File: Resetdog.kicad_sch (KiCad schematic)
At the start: 14 parts, among them U14 MC14541BD, U15 MC74HC4538ADG

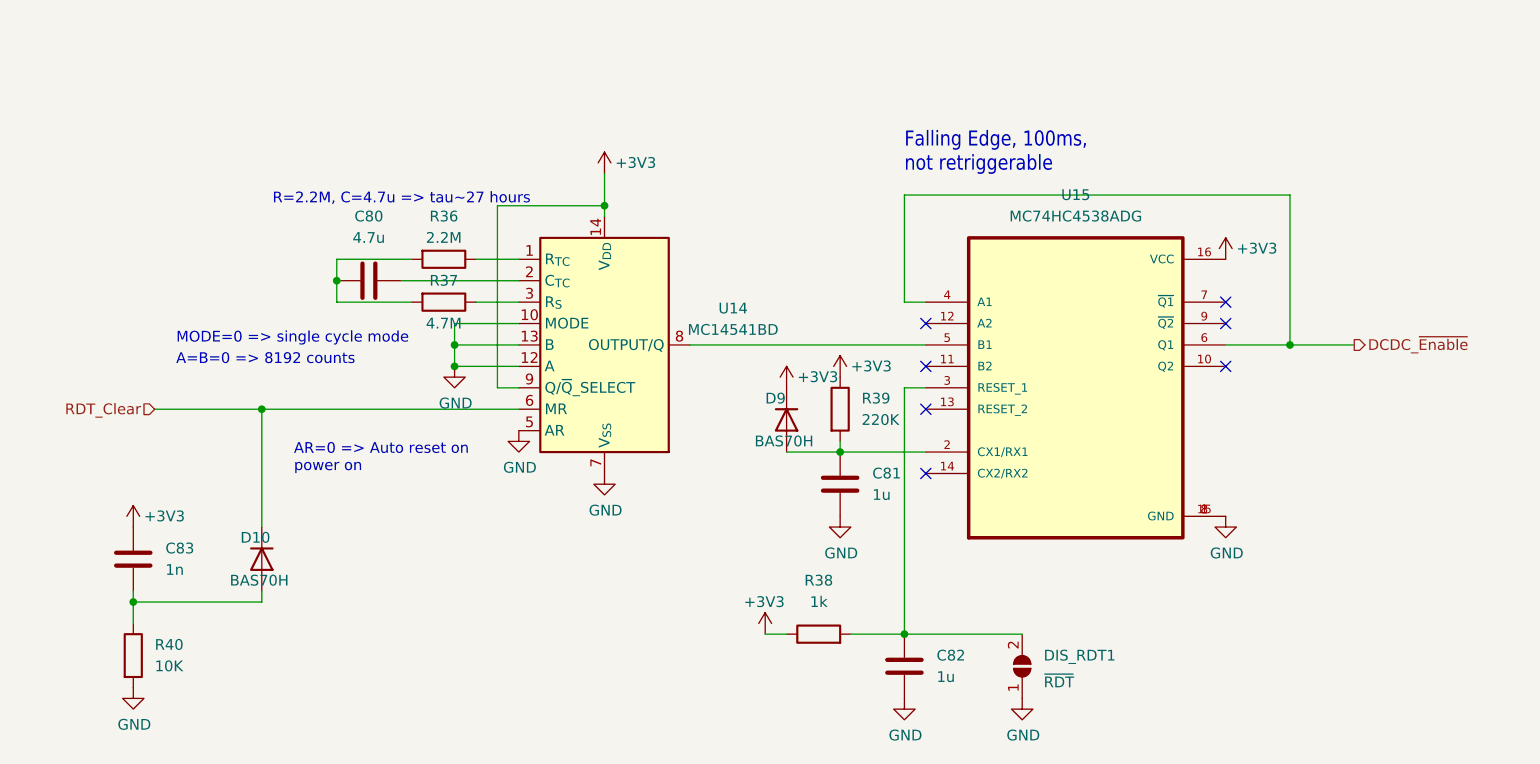
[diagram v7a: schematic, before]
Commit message: Make changes to the RDT: switch off AR, add Schmidt trigger for MR, change values of R40 and C83
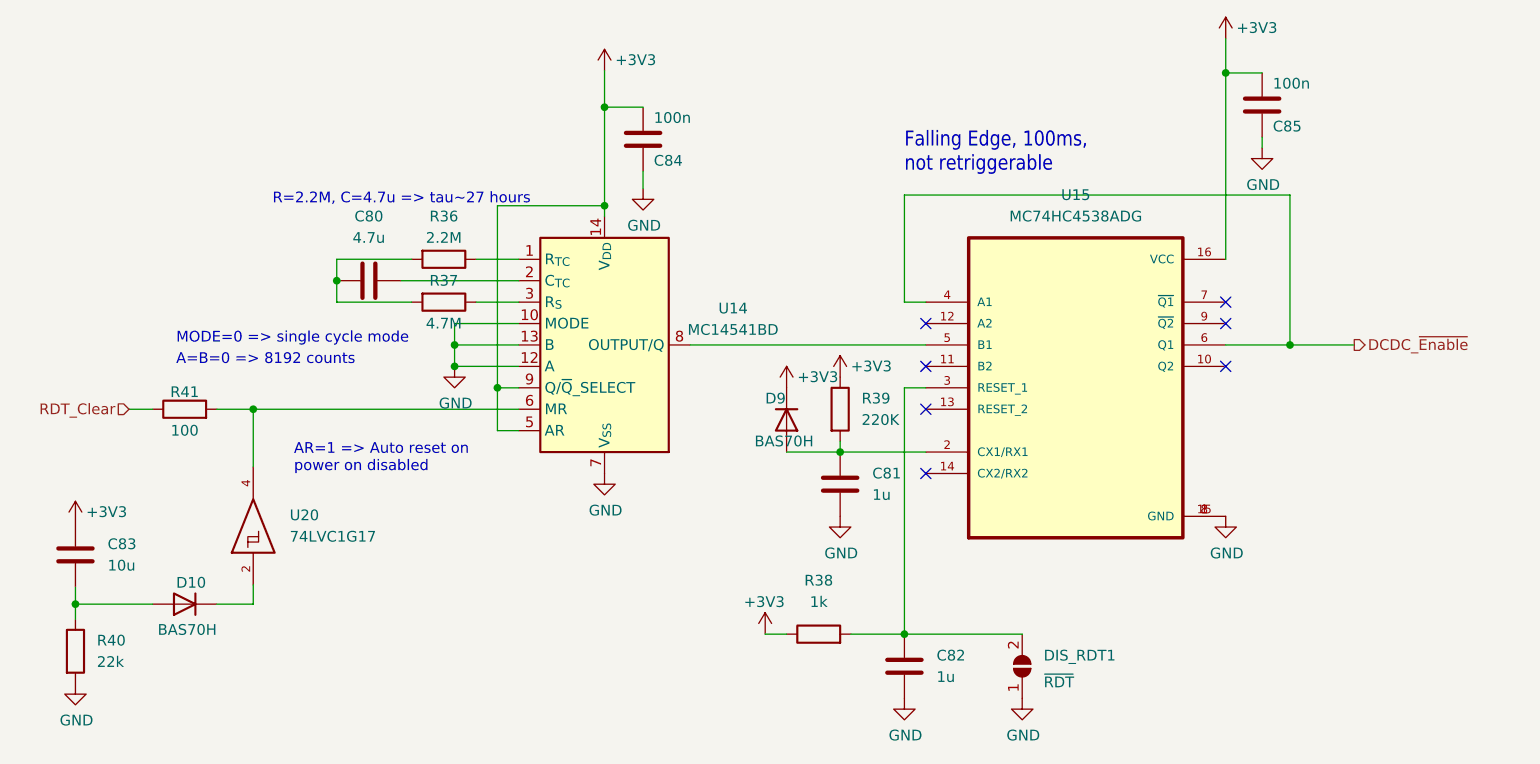
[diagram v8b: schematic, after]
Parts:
- added C84, C85: 100n, Capacitor_SMD:C_0603_1608Metric, symbol Device:C
- added R41: 100, Resistor_SMD:R_0603_1608Metric, symbol Device:R
- added U20: 74LVC1G17, Package_TO_SOT_SMD:SOT-23-5, symbol 74xGxx:74LVC1G17
- C83: value 1n -> 10u
- R40: value 10K -> 22k
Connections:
- net +3V3: now also U14.5 (AR), C84.2, C85.2
- net GND: now also C84.1, C85.1, U20.3 (GND); no longer U14.5 (AR)
- net RDT_Clear: now also R41.1; no longer D10.1 (K), U14.6 (MR)
- new net: R41.2, U14.6 (MR), U20.4
- new net: D10.1 (K), U20.2
- new net VCC: U20.5 (VCC)
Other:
- note added: "AR=1 => Auto reset on power on disabled"
- note removed: "AR=0 => Auto reset on power on"
- moved on the sheet: C83, D10, R40
